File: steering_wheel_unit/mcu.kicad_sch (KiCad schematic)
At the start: 42 parts, among them SW1 TL3305BF100QG, SW2 TL3305BF100QG, SW3 TL3305BF100QG, U1 STM32G491CCTx, U2 USBLC6-2P6, X1 32k768, X2 24M

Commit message: Add zones for gnd and power
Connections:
- net VREF: now reaches C7.1, C8.1, L2.2, U1.20 (VREF+)
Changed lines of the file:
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@@
+		)
+	)
+	(label "VREF"
+		(at 186.69 62.23 0)
+		(effects
+			(font
+				(size 1.27 1.27)
+			)
+			(justify left bottom)
 		)
 	)

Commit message: Add some routing changes
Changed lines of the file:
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@@
 	(wire
 		(pts
-			(xy 68.58 99.06) (xy 68.58 100.33)
+			(xy 68.58 97.79) (xy 68.58 100.33)
 		)
 		(stroke
@@
 	(symbol
 		(lib_id "power:+3.3V")
-		(at 68.58 99.06 0)
+		(at 68.58 97.79 0)
 		(unit 1)
 		(exclude_from_sim no)
@@
 		(dnp no)
 		(property "Reference" "#PWR025"
-			(at 68.58 102.87 0)
+			(at 68.58 101.6 0)
 			(effects
 				(font
@@
 		)
 		(property "Value" "+3.3V"
-			(at 68.58 94.615 0)
+			(at 68.58 93.345 0)
 			(effects
 				(font
@@
 		)
 		(property "Footprint" ""
-			(at 68.58 99.06 0)
+			(at 68.58 97.79 0)
 			(effects
 				(font
@@
 		)
 		(property "Datasheet" ""
-			(at 68.58 99.06 0)
+			(at 68.58 97.79 0)
 			(effects
 				(font
@@
 		)
 		(property "Description" ""
-			(at 68.58 99.06 0)
+			(at 68.58 97.79 0)
 			(effects
 				(font

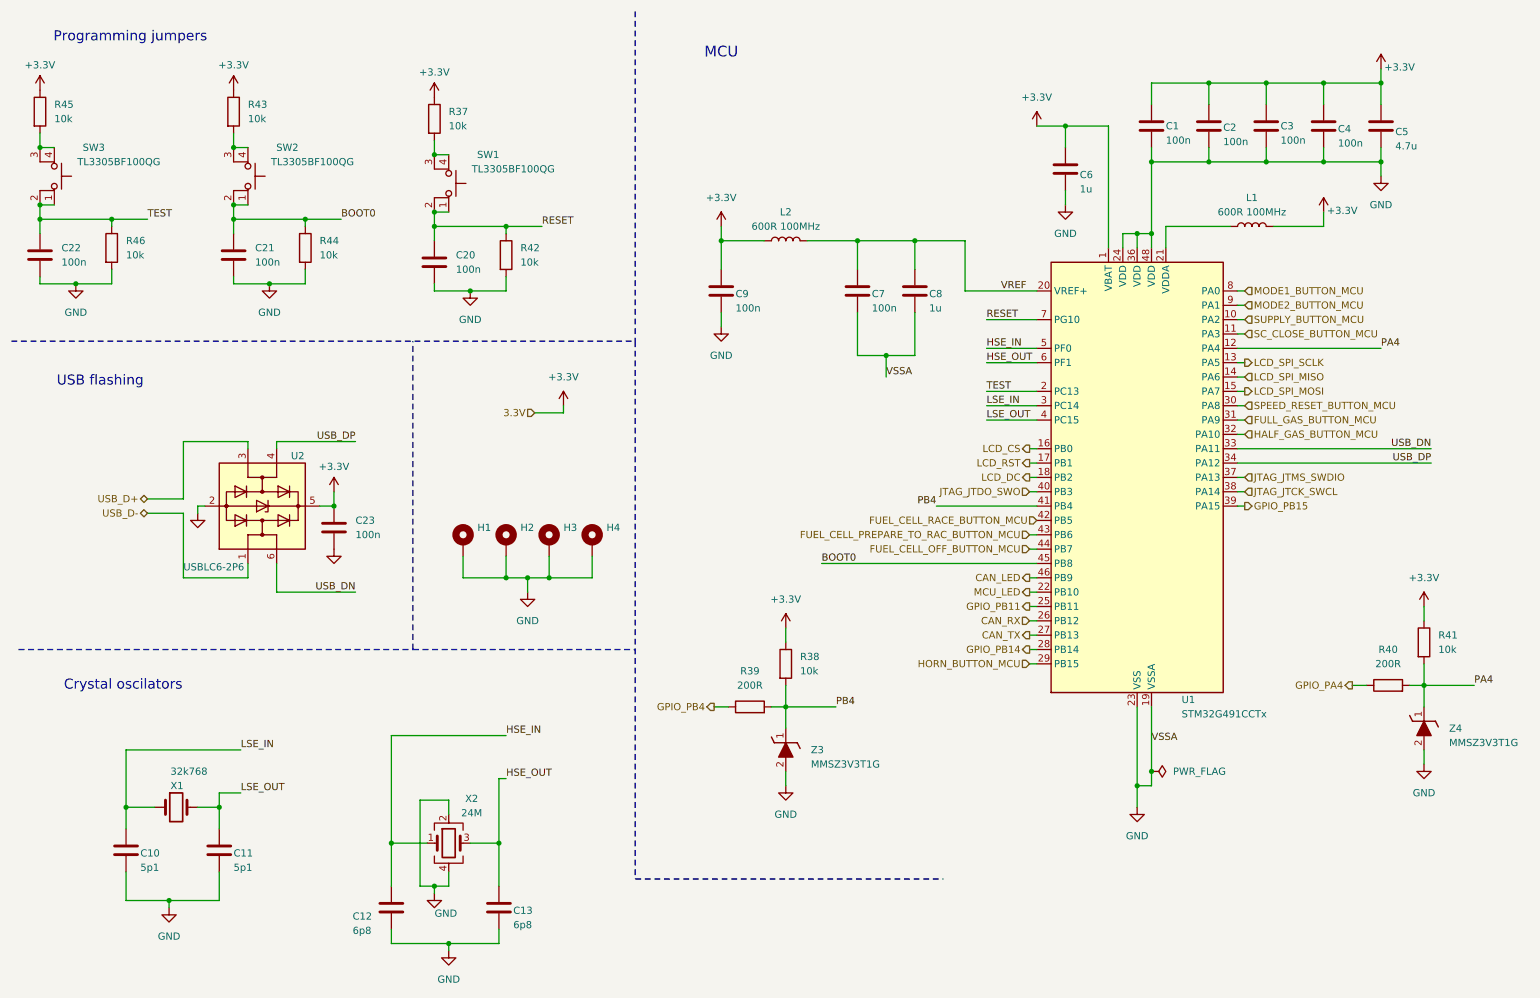
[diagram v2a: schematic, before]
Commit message: Edit tracks and add captions of elements
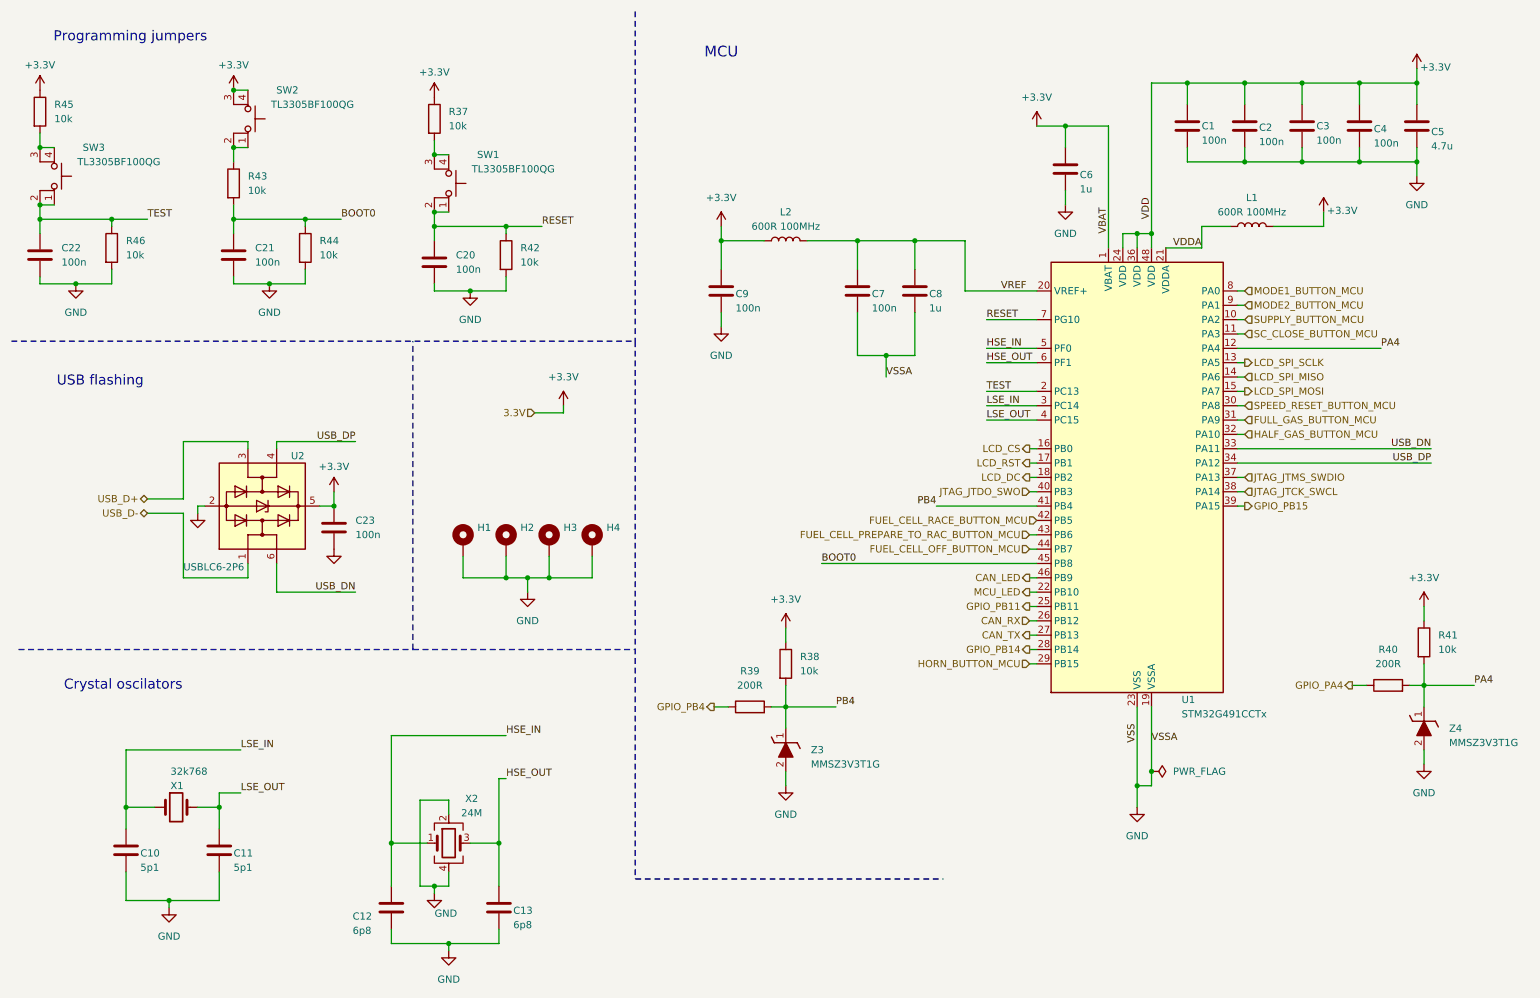
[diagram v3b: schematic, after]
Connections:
- net +3.3V: now also SW2.3 (K), SW2.4 (A), U1.24 (VDD), U1.36 (VDD), U1.48 (VDD); no longer R43.1
- net BOOT0: now also R43.2; no longer SW2.1, SW2.2
- net GND: no longer U1.24 (VDD), U1.36 (VDD), U1.48 (VDD)
- net VDDA: now reaches L1.1, U1.21 (VDDA)
- new net: R43.1, SW2.1, SW2.2
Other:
- moved on the sheet: C1, C2, C3, C4, C5, R43, SW2

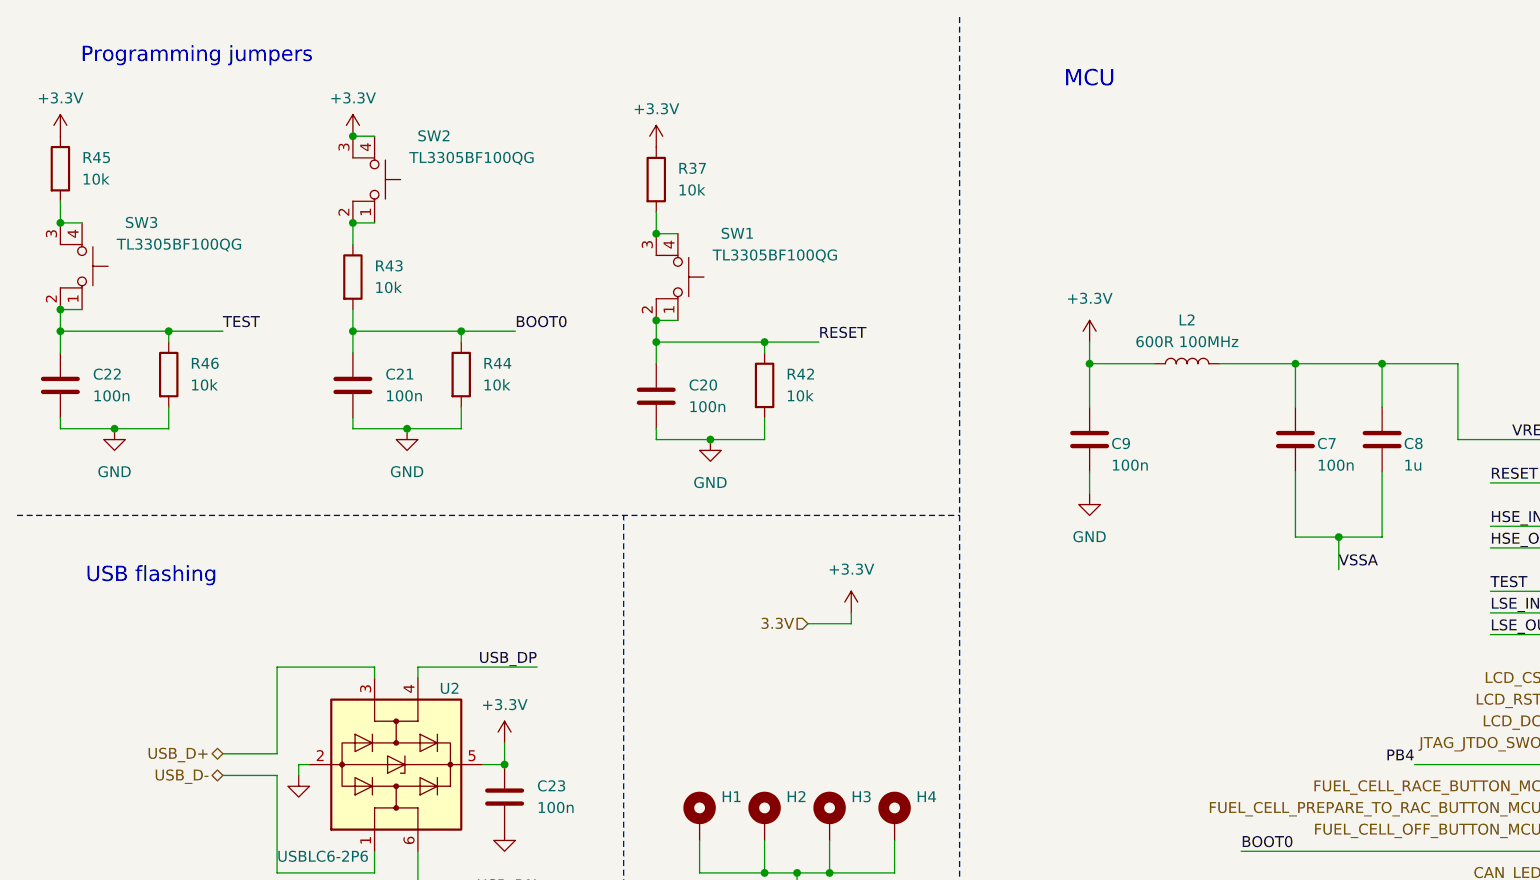
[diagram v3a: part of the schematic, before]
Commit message: Add dimensions
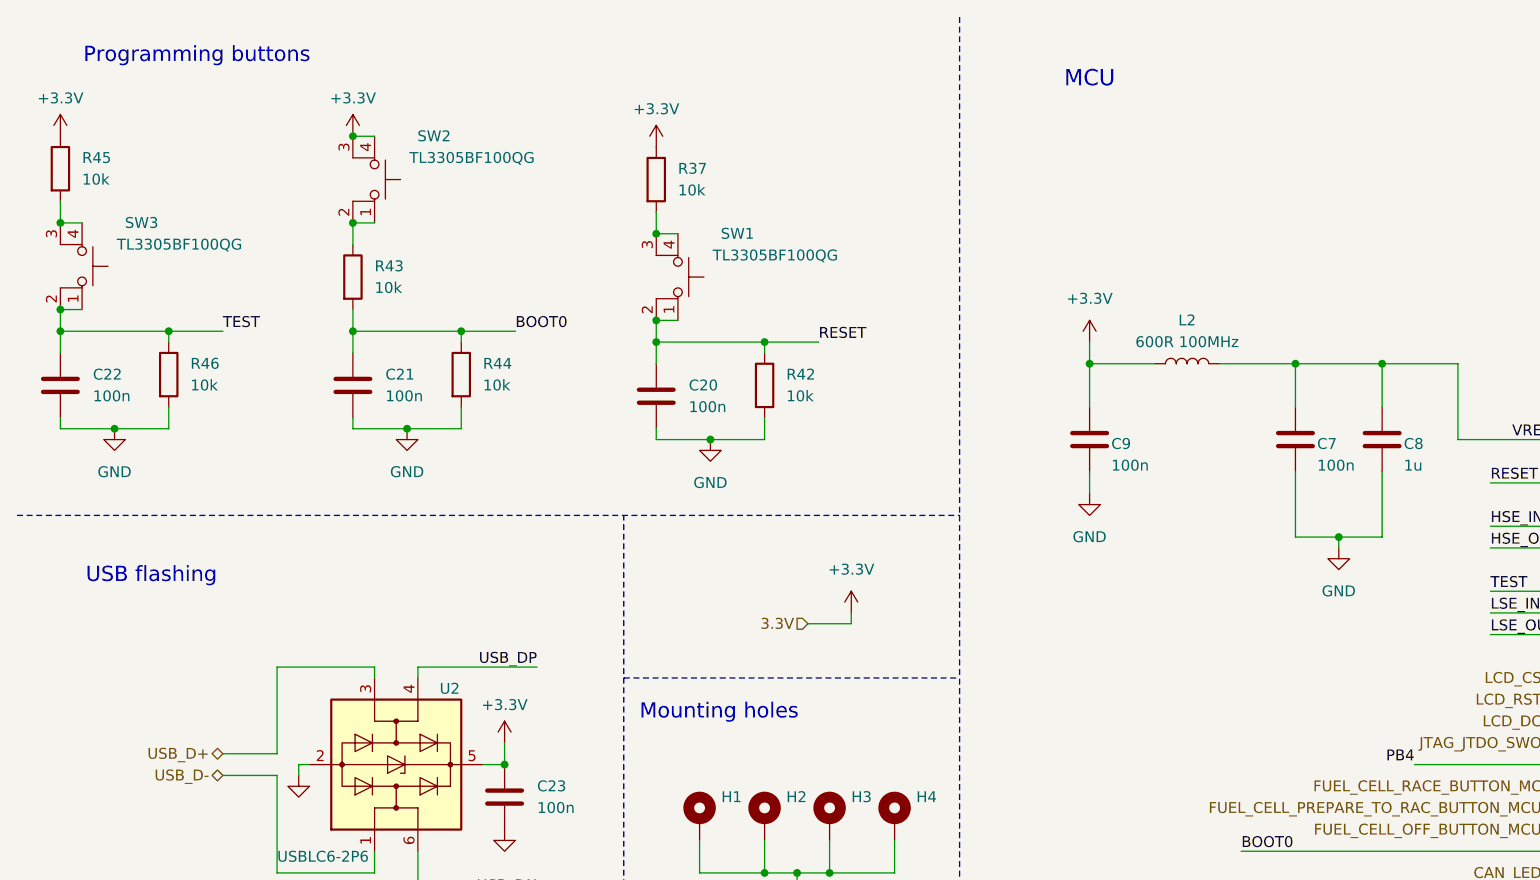
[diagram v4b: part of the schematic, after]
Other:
- note added: "Mounting holes"
- note added: "Programming buttons"
- note removed: "Programming jumpers"
- title: (none) -> Steering_wheel_unit_mcu
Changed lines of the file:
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@@
 	(generator_version "9.0")
 	(paper "A4")
+	(title_block
+		(title "Steering_wheel_unit_mcu")
+		(date "2025-03-22")
+	)
+	(text "Mounting holes\n"
+		(exclude_from_sim no)
+		(at 93.726 94.234 0)
+		(effects
+			(font
+				(size 1.778 1.778)
+			)
+		)
+	)
 	(text "MCU"
 		(exclude_from_sim no)
@@
 		)
 	)
-	(text "Programming jumpers"
+	(text "Programming buttons\n"
 		(exclude_from_sim no)
 		(at 32.512 17.272 0)
@@
 	(wire
 		(pts
-			(xy 166.37 73.66) (xy 166.37 77.47)
+			(xy 166.37 73.66) (xy 166.37 74.93)
 		)
 		(stroke
@@
 			(width 0)
 			(type default)
+		)
+	)
+	(polyline
+		(pts
+			(xy 82.55 90.17) (xy 121.92 90.17)
+		)
+		(stroke
+			(width 0)
+			(type dash)
 		)
 	)
@@
 	(label "HSE_OUT"
 		(at 184.15 74.93 0)
-		(effects
-			(font
-				(size 1.27 1.27)
-			)
-			(justify left bottom)
-		)
-	)
-	(label "VSSA"
-		(at 166.37 77.47 0)
 		(effects
 			(font
@@
 					(unit 1)
 				)
+			)
+		)
+	)
+	(symbol
+		(lib_id "power:GND")
+		(at 166.37 74.93 0)
+		(unit 1)
+		(exclude_from_sim no)
+		(in_bom yes)
+		(on_board yes)
+		(dnp no)
+		(fields_autoplaced yes)
+		(property "Reference" "#PWR067"
+			(at 166.37 81.28 0)
+			(effects
+				(font
+					(size 1.27 1.27)
+				)
+				(hide yes)
+			)
+		)
+		(property "Value" "GND"
+			(at 166.37 80.01 0)
+			(effects
+				(font
+					(size 1.27 1.27)
+				)
+			)
+		)
+		(property "Footprint" ""
+			(at 166.37 74.93 0)
+			(effects
+				(font
+					(size 1.27 1.27)
+				)
+				(hide yes)
+			)
+		)
+		(property "Datasheet" ""
+			(at 166.37 74.93 0)
+			(effects
+				(font
+					(size 1.27 1.27)
+				)
+				(hide yes)
+			)
+		)
+		(property "Description" "Power symbol creates a global label with name \"GND\" , ground"
+			(at 166.37 74.93 0)
+			(effects
+				(font
+					(size 1.27 1.27)
+				)
+				(hide yes)
+			)
+		)
+		(pin "1"
+		)
+		(instances
+			(project ""
+				(path "/b435671d-bfd7-4707-b36e-3eecb7fa1f89/49e3c9ae-cbf9-4f58-a1a3-484e0a637fd9"
+					(reference "#PWR067")
+					(unit 1)
+				)

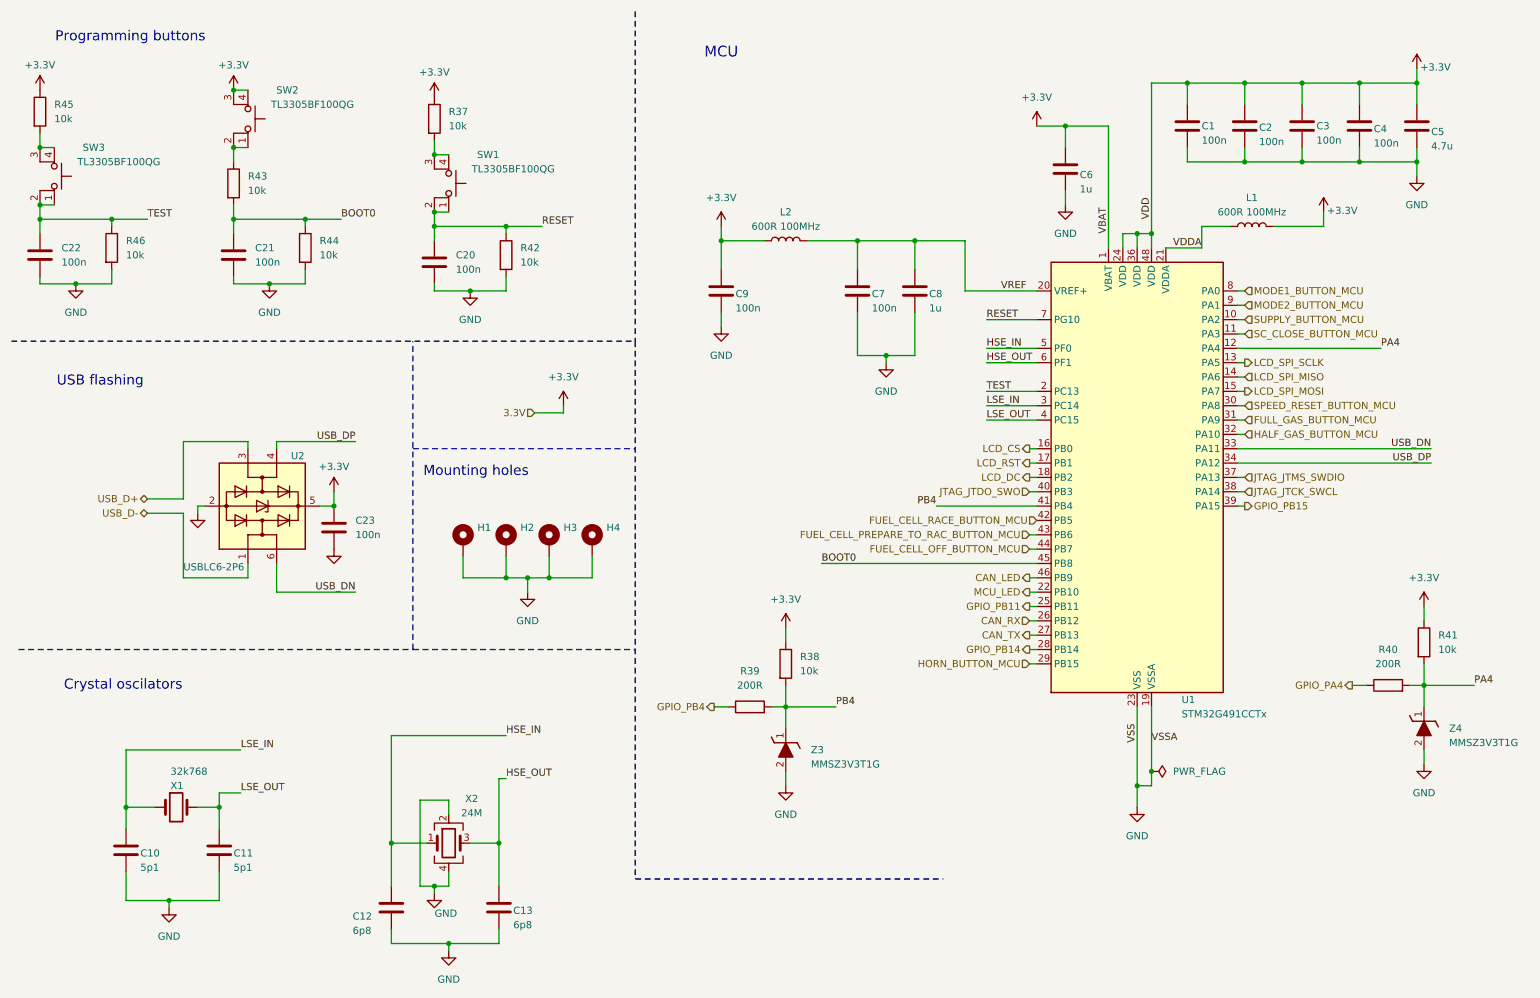
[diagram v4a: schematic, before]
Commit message: Add no GND zones and logo
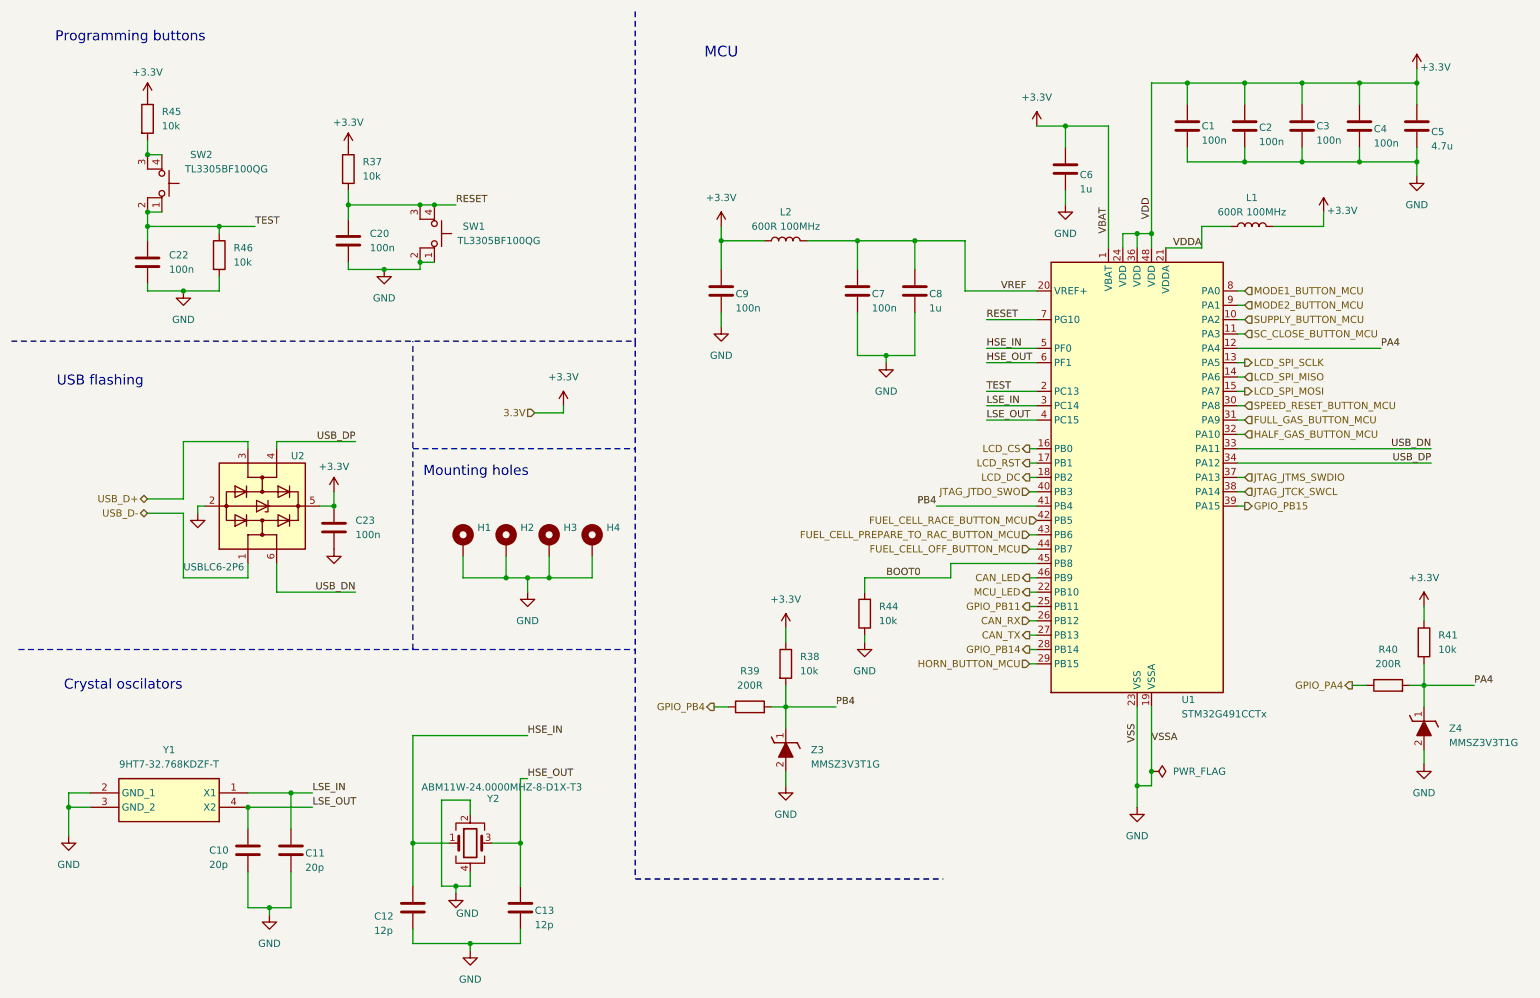
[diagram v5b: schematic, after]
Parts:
- removed C21: 100n, Capacitor_SMD:C_1206_3216Metric, symbol Device:C
- removed R42, R43: 10k, Resistor_SMD:R_1206_3216Metric, symbol Device:R
- removed SW2: TL3305BF100QG, Lib:SW_TL3305BF160QG, symbol Switch:SW_MEC_5E
- removed X1: 32k768, Lib:XTAL_NX3215SA-32.768K-STD-MUA-14, symbol Device:Crystal
- added Y1: 9HT7-32.768KDZF-T, 9HT732768KDZFT, symbol 9HT7-32_768KDZF-T:9HT7-32.768KDZF-T
- C10, C11: value 5p1 -> 20p
- C12, C13: value 6p8 -> 12p
- Y2: renamed from X2; value 24M -> ABM11W-24.0000MHZ-8-D1X-T3; footprint Lib:OSC_NX2016SA-24MHZ-EXS00A-CS10820 -> Lib:XTAL_ABM11W-24.0000MHZ-8-D1X-T3
- renumbered SW3 to SW2
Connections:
- net BOOT0: now also R44.2; no longer R44.1
- net GND: now also R44.1, SW1.1, SW1.2, Y1.2 (GND_1), Y1.3 (GND_2); no longer R44.2
- net LSE_IN: now also C11.1, Y1.1 (X1); no longer C10.1
- net LSE_OUT: now also C10.1, Y1.4 (X2); no longer C11.1
- net RESET: now also R37.2, SW1.3 (K), SW1.4 (A); no longer SW1.1, SW1.2
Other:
- moved on the sheet: C10, C11, C12, C13, C20, C22, R37, R44, R45, R46, SW1, SW2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
